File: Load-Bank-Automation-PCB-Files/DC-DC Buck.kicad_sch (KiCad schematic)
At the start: 28 parts, among them Q1 NMOS, Q2 NMOS, U1 LM25145RGYT

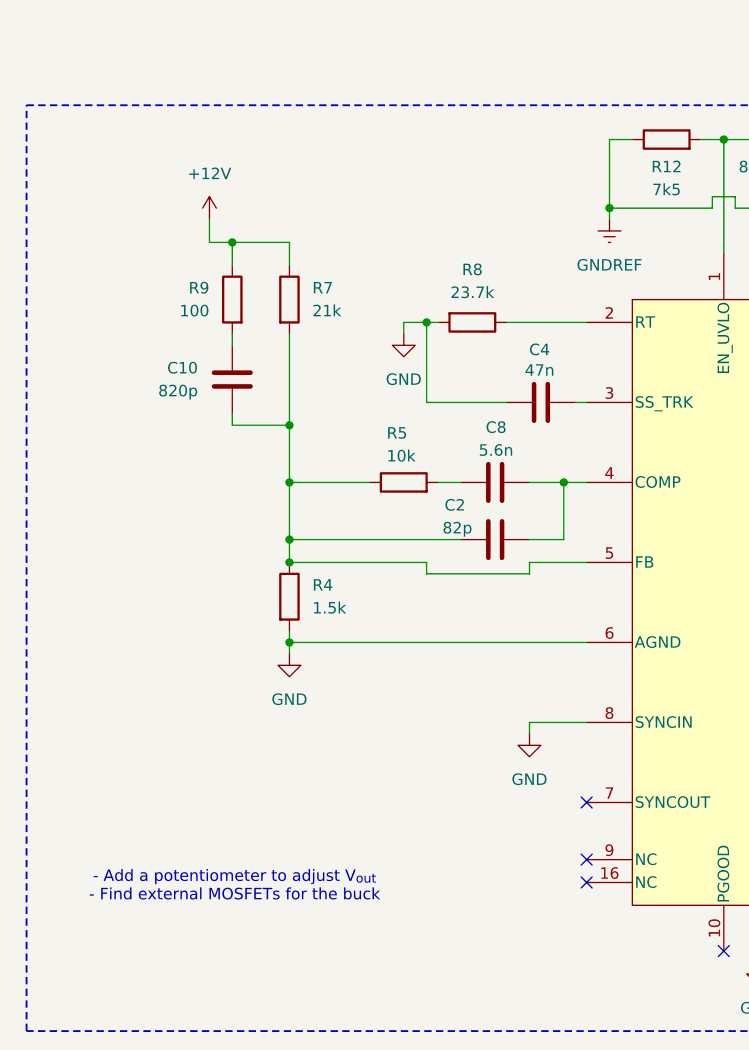
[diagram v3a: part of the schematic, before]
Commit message: Added potentiometer to buck converter and New schematic for MOSFET boards
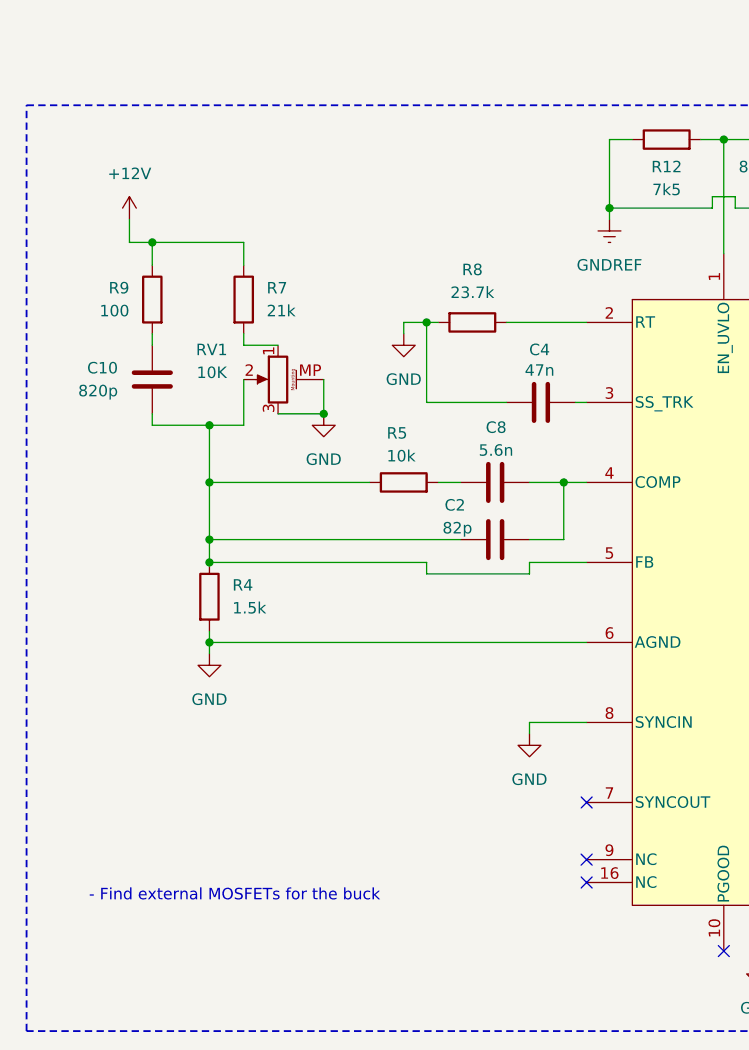
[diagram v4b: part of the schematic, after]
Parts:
- added RV1: 10K, Potentiometer_THT:Potentiometer_Bourns_PTV09A-4_Single_Vertical, symbol Device:R_Potentiometer_MountingPin
- C1, C10, C2, C20, C25, C26, C27, C28, C29, C3, C30, C31, C4, C6, C7, C8: footprint Resistor_SMD:R_0603_1608Metric -> Capacitor_SMD:C_0603_1608Metric
- L1: footprint Resistor_SMD:R_0603_1608Metric -> Inductor_SMD:L_0603_1608Metric
- U1: footprint RGY0020B -> Package_DFN_QFN:Texas_RGY_R-PVQFN-N20_EP2.05x3.05mm_ThermalVias
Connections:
- net GND: now also RV1.3, RV1.MP (MountPin)
- net at C10.2, C2.1, R4.1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: now also RV1.2; no longer R7.2
- new net: R7.2, RV1.1
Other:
- note added: "- Find external MOSFETs for the buck"
- note removed: "- Add a potentiometer to adjust V_{out} - Find external MOSFETs for the buck"
- moved on the sheet: C10, R4, R7, R9

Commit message: Schematic revision for review
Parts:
- Q1, Q2: value NMOS -> CSD18543Q3A
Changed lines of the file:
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@@
 	)
 	(junction
+		(at 203.2 78.74)
+		(diameter 0)
+		(color 0 0 0 0)
+	)
+	(junction
 		(at 184.15 52.07)
 		(diameter 0)
@@
 	)
 	(junction
+		(at 172.72 96.52)
+		(diameter 0)
+		(color 0 0 0 0)
+	)
+	(junction
 		(at 104.14 60.96)
 		(diameter 0)
@@
 	)
 	(junction
-		(at 184.15 44.45)
-		(diameter 0)
-		(color 0 0 0 0)
-	)
-	(junction
 		(at 137.16 40.64)
 		(diameter 0)
@@
 	(wire
 		(pts
+			(xy 203.2 78.74) (xy 209.55 78.74)
+		)
+		(stroke
+			(width 0)
+			(type default)
+		)
+	)
+	(wire
+		(pts
 			(xy 148.59 48.26) (xy 152.4 48.26)
 		)
@@
 	(wire
 		(pts
+			(xy 203.2 74.93) (xy 203.2 78.74)
+		)
+		(stroke
+			(width 0)
+			(type default)
+		)
+	)
+	(wire
+		(pts
 			(xy 80.01 95.25) (xy 80.01 96.52)
 		)
@@
 	(wire
 		(pts
-			(xy 184.15 44.45) (xy 184.15 43.18)
+			(xy 184.15 43.18) (xy 184.15 48.26)
 		)
 		(stroke
@@
 	(wire
 		(pts
-			(xy 184.15 48.26) (xy 184.15 44.45)
-		)
-		(stroke
-			(width 0)
-			(type default)
-		)
-	)
-	(wire
-		(pts
 			(xy 73.66 72.39) (xy 73.66 71.12)
 		)
@@
 	(wire
 		(pts
-			(xy 184.15 44.45) (xy 186.69 44.45)
-		)
-		(stroke
-			(width 0)
-			(type default)
-		)
-	)
-	(wire
-		(pts
 			(xy 80.01 85.09) (xy 80.01 87.63)
 		)
@@
 	(wire
 		(pts
-			(xy 196.85 78.74) (xy 209.55 78.74)
+			(xy 196.85 78.74) (xy 203.2 78.74)
 		)
 		(stroke
@@
 	(wire
 		(pts
+			(xy 172.72 88.9) (xy 172.72 96.52)
+		)
+		(stroke
+			(width 0)
+			(type default)
+		)
+	)
+	(wire
+		(pts
 			(xy 119.38 85.09) (xy 115.57 85.09)
 		)
@@
 	)
 	(symbol
+		(lib_id "power:PWR_FLAG")
+		(at 203.2 74.93 0)
+		(unit 1)
+		(exclude_from_sim no)
+		(in_bom yes)
+		(on_board yes)
+		(dnp no)
+		(fields_autoplaced yes)
+		(property "Reference" "#FLG03"
+			(at 203.2 73.025 0)
+			(effects
+				(font
+					(size 1.27 1.27)
+				)
+				(hide yes)
+			)
+		)
+		(property "Value" "PWR_FLAG"
+			(at 203.2 69.85 0)
+			(effects
+				(font
+					(size 1.27 1.27)
+				)
+			)
+		)
+		(property "Footprint" ""
+			(at 203.2 74.93 0)
+			(effects
+				(font
+					(size 1.27 1.27)
+				)
+				(hide yes)
+			)
+		)
+		(property "Datasheet" "~"
+			(at 203.2 74.93 0)
+			(effects
+				(font
+					(size 1.27 1.27)
+				)
+				(hide yes)
+			)
+		)
+		(property "Description" "Special symbol for telling ERC where power comes from"
+			(at 203.2 74.93 0)
+			(effects
+				(font
+					(size 1.27 1.27)
+				)
+				(hide yes)
+			)
+		)
+		(pin "1"
+		)
+		(instances
+			(project ""
+				(path "/c82c4769-33eb-46b7-8d07-39045014a3da/eb9b9647-818b-4f6a-aec9-7481a1a3b43c/36fe7d56-cf73-41f9-a092-e3a444c4baa1"
+					(reference "#FLG03")
+					(unit 1)
+				)
+			)
+		)
+	)
+	(symbol
 		(lib_id "Device:C")
 		(at 199.39 116.84 90)
@@
 		(dnp no)
 		(property "Reference" "Q1"
-			(at 186.944 90.17 0)
+			(at 184.404 96.52 0)
 			(effects
 				(font
@@
 			)
 		)
-		(property "Value" "NMOS"
-			(at 186.944 92.71 0)
+		(property "Value" "CSD18543Q3A"
+			(at 184.404 99.06 0)
 			(effects
 				(font
-					(size 1.27 1.27)
+					(size 1.016 1.016)
 				)
 				(justify left)
@@
 	)
 	(symbol
+		(lib_id "power:PWR_FLAG")
+		(at 172.72 88.9 0)
+		(unit 1)
+		(exclude_from_sim no)
+		(in_bom yes)
+		(on_board yes)
+		(dnp no)
+		(fields_autoplaced yes)
+		(property "Reference" "#FLG06"
+			(at 172.72 86.995 0)
+			(effects
+				(font
+					(size 1.27 1.27)
+				)
+				(hide yes)
+			)
+		)
+		(property "Value" "PWR_FLAG"
+			(at 172.72 83.82 0)
+			(effects
+				(font
+					(size 1.27 1.27)
+				)
+			)
+		)
+		(property "Footprint" ""
+			(at 172.72 88.9 0)
+			(effects
+				(font
+					(size 1.27 1.27)
+				)
+				(hide yes)
+			)
+		)
+		(property "Datasheet" "~"
+			(at 172.72 88.9 0)
+			(effects
+				(font
+					(size 1.27 1.27)
+				)
+				(hide yes)
+			)
+		)
+		(property "Description" "Special symbol for telling ERC where power comes from"
+			(at 172.72 88.9 0)
+			(effects
+				(font
+					(size 1.27 1.27)
+				)
+				(hide yes)
+			)
+		)
+		(pin "1"
+		)
+		(instances
+			(project "Main Board"
+				(path "/c82c4769-33eb-46b7-8d07-39045014a3da/eb9b9647-818b-4f6a-aec9-7481a1a3b43c/36fe7d56-cf73-41f9-a092-e3a444c4baa1"
+					(reference "#FLG06")
+					(unit 1)
+				)
+			)
+		)
+	)
+	(symbol
 		(lib_id "Device:C")
 		(at 199.39 96.52 90)
@@
 		(dnp no)
 		(property "Reference" "Q2"
-			(at 186.944 68.58 0)
+			(at 184.404 61.214 0)
 			(effects
 				(font
@@
 			)
 		)
-		(property "Value" "NMOS"
-			(at 186.944 71.12 0)
+		(property "Value" "CSD18543Q3A"
+			(at 184.404 63.754 0)
 			(effects
 				(font
-					(size 1.27 1.27)
+					(size 1.016 1.016)
 				)
 				(justify left)
@@
 					(unit 1)
 				)
-			)
-		)
-	)
-	(symbol
-		(lib_id "power:PWR_FLAG")
-		(at 186.69 44.45 0)
-		(unit 1)
-		(exclude_from_sim no)
-		(in_bom yes)
-		(on_board yes)
-		(dnp no)
-		(fields_autoplaced yes)
-		(property "Reference" "#FLG03"
-			(at 186.69 42.545 0)
-			(effects
-				(font
-					(size 1.27 1.27)
-				)
-				(hide yes)
-			)
-		)
-		(property "Value" "PWR_FLAG"
-			(at 186.69 39.37 0)
-			(effects
-				(font
-					(size 1.27 1.27)
-				)
-			)
-		)
-		(property "Footprint" ""
-			(at 186.69 44.45 0)
-			(effects
-				(font
-					(size 1.27 1.27)
-				)
-				(hide yes)
-			)
-		)
-		(property "Datasheet" "~"
-			(at 186.69 44.45 0)
-			(effects
-				(font
-					(size 1.27 1.27)
-				)
-				(hide yes)
-			)
-		)
-		(property "Description" "Special symbol for telling ERC where power comes from"
-			(at 186.69 44.45 0)
-			(effects
-				(font
-					(size 1.27 1.27)
-				)
-				(hide yes)
-			)
-		)
-		(pin "1"
-		)
-		(instances
-			(project "Main Board"
-				(path "/c82c4769-33eb-46b7-8d07-39045014a3da/eb9b9647-818b-4f6a-aec9-7481a1a3b43c/36fe7d56-cf73-41f9-a092-e3a444c4baa1"
-					(reference "#FLG03")
-					(unit 1)
-				)

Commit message: Saving Progress (Changed eFuse and comments)
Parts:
- removed C10: 820p, Capacitor_SMD:C_0603_1608Metric, symbol Device:C
- removed C20, C25, C26: 10u, Capacitor_SMD:C_0603_1608Metric, symbol Device:C
- removed C27, C28, C29, C7: 22u, Capacitor_SMD:C_0603_1608Metric, symbol Device:C
- removed C30: 12p, Capacitor_SMD:C_0603_1608Metric, symbol Device:C
- removed C31: 100n, Capacitor_SMD:C_0603_1608Metric, symbol Device:C
- removed C8: 5.6n, Capacitor_SMD:C_0603_1608Metric, symbol Device:C
- removed Q1, Q2: CSD18543Q3A, symbol Simulation_SPICE:NMOS
- removed R11: 80k6, Resistor_SMD:R_0603_1608Metric, symbol Device:R
- removed R12: 7k5, Resistor_SMD:R_0603_1608Metric, symbol Device:R
- removed R9: 100, Resistor_SMD:R_0603_1608Metric, symbol Device:R
- removed RV1: 10K, Potentiometer_THT:Potentiometer_Bourns_PTV09A-4_Single_Vertical, symbol Device:R_Potentiometer_MountingPin
- removed U1: LM25145RGYT, Package_DFN_QFN:Texas_RGY_R-PVQFN-N20_EP2.05x3.05mm_ThermalVias, symbol LM25145RGYT:LM25145RGYT
- added U48: TPS62933F, Package_TO_SOT_SMD:SOT-583-8, symbol Regulator_Switching:TPS62933F
- C1: value 2200n -> 100n; footprint Capacitor_SMD:C_0603_1608Metric -> Capacitor_SMD:C_0201_0603Metric_Pad0.64x0.40mm_HandSolder
- C2: value 82p -> 47u; footprint Capacitor_SMD:C_0603_1608Metric -> Capacitor_SMD:C_1210_3225Metric_Pad1.33x2.70mm_HandSolder
- C3: value 100n -> 180n; footprint Capacitor_SMD:C_0603_1608Metric -> Capacitor_SMD:C_0603_1608Metric_Pad1.08x0.95mm_HandSolder
- C4: value 47n -> 100n; footprint Capacitor_SMD:C_0603_1608Metric -> Capacitor_SMD:C_0603_1608Metric_Pad1.08x0.95mm_HandSolder
- C6: footprint Capacitor_SMD:C_0603_1608Metric -> Capacitor_SMD:C_1210_3225Metric_Pad1.33x2.70mm_HandSolder
- L1: value 5600n -> 15u; footprint Inductor_SMD:L_0603_1608Metric -> Inductor_SMD:L_Bourns_SRR1260
- R4: value 1.5k -> 56.2k; footprint Resistor_SMD:R_0603_1608Metric -> Resistor_SMD:R_0402_1005Metric_Pad0.72x0.64mm_HandSolder
- R5: value 10k -> 140k; footprint Resistor_SMD:R_0603_1608Metric -> Resistor_SMD:R_0603_1608Metric_Pad0.98x0.95mm_HandSolder
- R6: value 500 -> 10k; footprint Resistor_SMD:R_0603_1608Metric -> Resistor_SMD:R_0402_1005Metric_Pad0.72x0.64mm_HandSolder
- R7: value 21k -> 698k; footprint Resistor_SMD:R_0603_1608Metric -> Resistor_SMD:R_0402_1005Metric_Pad0.72x0.64mm_HandSolder
- R8: value 23.7k -> 60.4k; footprint Resistor_SMD:R_0603_1608Metric -> Resistor_SMD:R_0402_1005Metric_Pad0.72x0.64mm_HandSolder
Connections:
- net GNDREF is gone; now on net GND: C6.2
- net +12V: now also C2.1, R5.1; no longer R7.1
- net GND: now also C2.2, C3.2, C4.2, R6.2, U48.4 (GND); no longer C1.2, C4.1
- net Protected_18V: now also C4.1, R7.1, U48.3 (VIN)
- net at C3.1: now also U48.7 (SS)
- net at L1.1: now also C1.2, U48.5 (SW); no longer C3.2
- net at R5.2: now also R6.1, U48.8 (FB)
- net at R8.1: now also R7.2, U48.2 (EN)
- net at C1.1: now also U48.6 (BST)
- new net: R4.1, U48.1 (RT)
- no-connect marks 6 -> 0
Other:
- note added: "- I'm concerned that My delta I_{L} is significantly bigger than my rms I_{L}, would that cause a great issue?"
- note added: "Did many caluclations by hand and confirms some values"
- note added: "FCCM Buck Converter"
- note added: "V_{IN_MAX} = 30 V V_{UVLO(Rise)} = 15 V I_{OUT_MAX} = 2.5 A t_{SS} = 25 ms f_{sw} = 389 KHz"
- note added: "https://webench.ti.com/appinfo/webench/scripts/SDP.cgi?ID=7F6EE7E642FA3575"
- note removed: "- Find external MOSFETs for the buck"

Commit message: Schematic for revision
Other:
- note added: "- I'm concerned that My delta I_{L} is significantly bigger than my rms I_{L}, is that normal?"
- note removed: "- I'm concerned that My delta I_{L} is significantly bigger than my rms I_{L}, would that cause a great issue?"
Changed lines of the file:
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@@
 		)
 	)
-	(text "- I'm concerned that My delta I_{L} is significantly bigger than my rms I_{L}, would that cause a great issue?\n"
+	(text "- I'm concerned that My delta I_{L} is significantly bigger than my rms I_{L}, is that normal?\n"
 		(exclude_from_sim no)
-		(at 231.14 171.45 0)
+		(at 222.504 169.926 0)
 		(effects
 			(font
